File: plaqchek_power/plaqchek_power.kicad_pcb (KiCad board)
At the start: 4 copper layers, 52 x 70 mm, 93 parts, among them J1 Conn_01x05, J2 Conn_01x04, J3 Barrel_Jack_Switch, J4 Conn_01x03, U1 LM5157, U2 LM43601, U8 TPS54202DDC, U9 TPS62175DQC

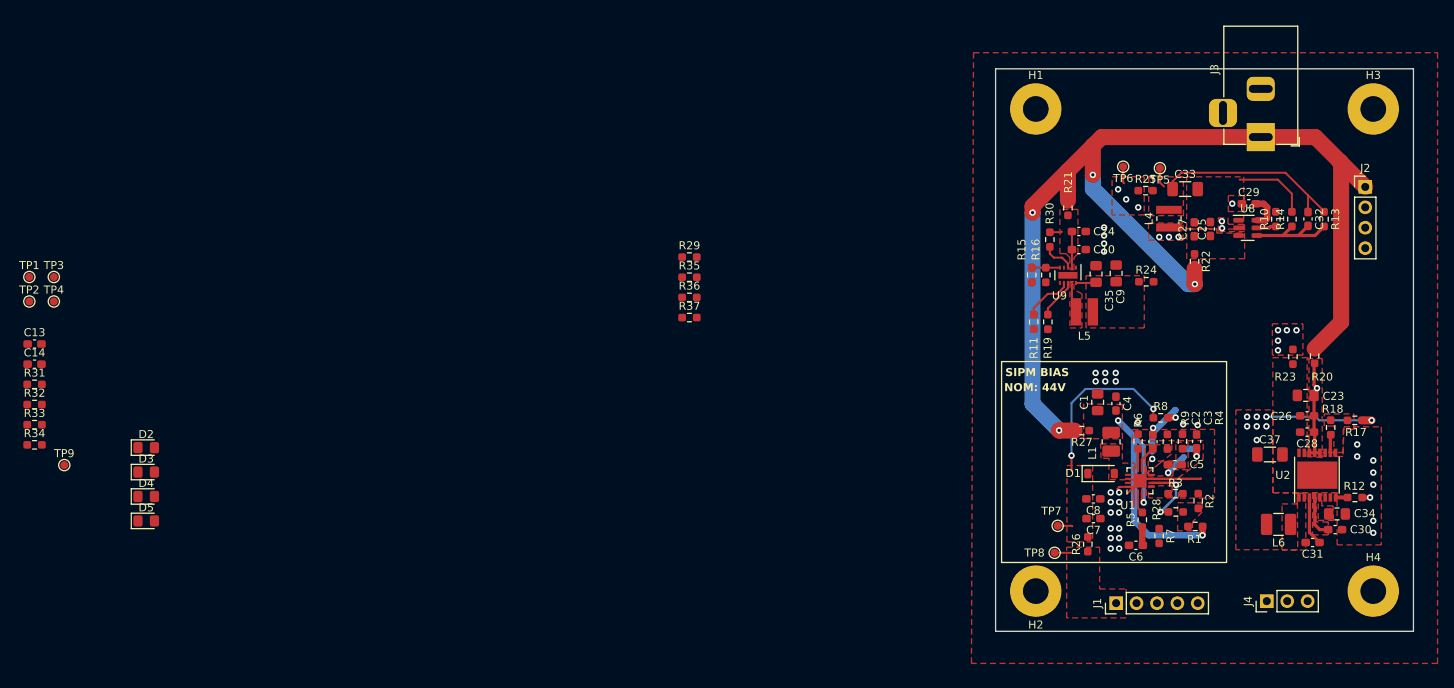
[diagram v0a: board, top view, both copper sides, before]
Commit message: minor silkscreen additions
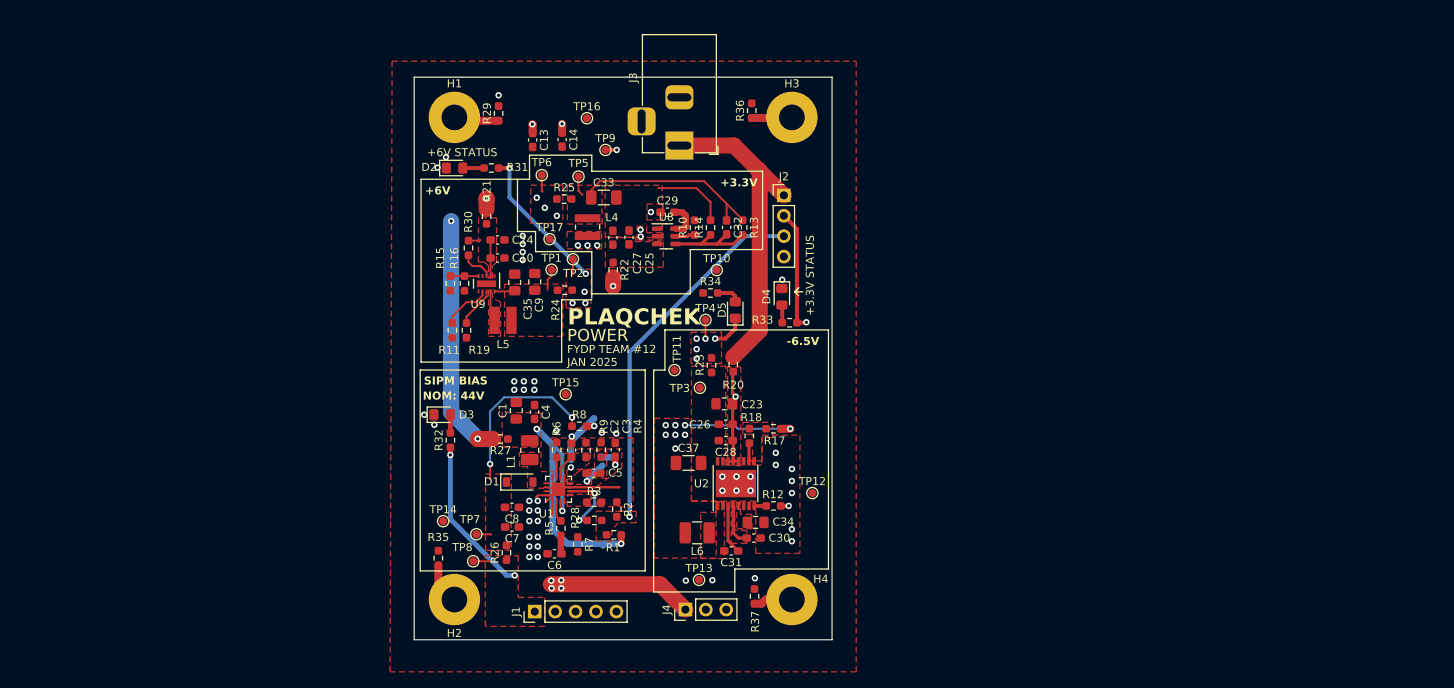
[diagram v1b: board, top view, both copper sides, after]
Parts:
- added TP10: TestPoint, TestPoint:TestPoint_Pad_D1.0mm, F.Cu at (160.3, 82.0)
- added TP11: TestPoint, TestPoint:TestPoint_Pad_D1.0mm, F.Cu at (155.1, 94.5)
- added TP12: TestPoint, TestPoint:TestPoint_Pad_D1.0mm, F.Cu at (172.2, 109.8)
- added TP13: TestPoint, TestPoint:TestPoint_Pad_D1.0mm, F.Cu at (158.1, 120.6)
- added TP14: TestPoint, TestPoint:TestPoint_Pad_D1.0mm, F.Cu at (126.2, 113.3)
- added TP15: TestPoint, TestPoint:TestPoint_Pad_D1.0mm, F.Cu at (141.5, 97.5)
- added TP16: TestPoint, TestPoint:TestPoint_Pad_D1.0mm, F.Cu at (144.2, 63.1)
- added TP17: TestPoint, TestPoint:TestPoint_Pad_D1.0mm, F.Cu at (139.5, 78.2)
- moved R33 94.8 mm to (169.4, 88.6), turned to 180 degrees
- moved R34 86.2 mm to (159.5, 84.9)
- moved D4 82.9 mm to (168.4, 85.4), turned to -90 degrees
- moved TP3 81.6 mm to (158.2, 96.7)
- moved TP4 81.1 mm to (158.9, 88.2)
- moved TP9 77.9 mm to (146.4, 67.1)
- moved D5 77.9 mm to (162.6, 87.0), turned to 90 degrees
- moved C10 72.4 mm to (133.0, 80.5)
- moved C24 72.4 mm to (133.0, 78.3)
- moved C33 72.4 mm to (146.2, 73.0)
- moved C34 72.4 mm to (165.1, 113.5)
- moved C5 72.4 mm to (144.9, 107.3)
- moved C7 72.4 mm to (134.8, 114.0)
- moved L5 72.4 mm to (133.7, 88.3)
- moved R27 72.4 mm to (133.4, 103.1)
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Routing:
- net +12V: track 132.2 -> 77.0 mm, vias 4 -> 7
- net PD_EN: track 0.00 -> 45.7 mm, vias 0 -> 1
- net +6V: track 0.00 -> 38.4 mm, vias 0 -> 9
- net SIPM_BIAS_OUT: track 2.10 -> 21.9 mm, vias 0 -> 2
- net +3V3: track 2.12 -> 17.3 mm, vias 3 -> 4
- net -6V5: track 0.00 -> 6.65 mm
- net Net-(H1-Pad1): track 0.00 -> 5.67 mm
- net Net-(H2-Pad1): track 0.00 -> 5.08 mm
- net Net-(H3-Pad1): track 0.00 -> 5.03 mm
- net Net-(H4-Pad1): track 0.00 -> 4.86 mm
- net Net-(D5-A): track 0.00 -> 3.04 mm
- net /main_pwr/VOUT_6V: track 2.53 -> 5.24 mm
- net Net-(D2-A): track 0.00 -> 2.64 mm
- net Net-(D4-A): track 0.00 -> 2.29 mm
- net Net-(D3-A): track 0.00 -> 2.25 mm
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- added copper zone on In2.Cu, net +12V
- added copper zone on F.Cu, net +6V
- added copper zone on In2.Cu, net +6V
- added copper zone on In2.Cu, net -6V5
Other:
- board text added: "+3.3V"
- board text added: "+3.3V STATUS"
- board text added: "+6V"
- board text added: "+6V STATUS"
- board text added: "-6.5V"
- board text added: "FYDP TEAM #12 JAN 2025"
- board text added: "PLAQCHEK"
- board text added: "POWER"

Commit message: finish all pcbs, generate gerber files
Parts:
- moved TP12 13.8 mm to (169.7, 96.2)
- moved TP13 9.67 mm to (166.6, 115.9)
- moved C1 2.64 mm to (134.0, 97.3)
- moved C10 2.64 mm to (131.6, 78.3)
- moved C13 2.64 mm to (136.0, 63.6)
- moved C14 2.64 mm to (139.7, 63.6)
- moved C2 2.64 mm to (140.9, 102.2)
- moved C23 2.64 mm to (159.9, 96.4)
- moved C24 2.64 mm to (131.6, 76.0)
- moved C25 2.64 mm to (148.0, 75.7)
- moved C26 2.64 mm to (160.0, 99.0)
- moved C27 2.64 mm to (146.0, 75.8)
- moved C28 2.64 mm to (160.0, 101.0)
- moved C29 2.64 mm to (152.8, 72.6)
- moved C3 2.64 mm to (146.3, 102.2)
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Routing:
- net /main_pwr/VOUT_6V: track 5.24 -> 19.9 mm, vias 0 -> 2
- net /SIPM Bias/VOUT_SIPM: track 23.4 -> 36.4 mm, vias 2 -> 4
- net /SIPM Bias/PD_BOOST_PG: track 0.00 -> 5.47 mm
- net /main_pwr/VOUT_-6V5: track 2.26 -> 5.44 mm, vias 13 -> 0
- net +12V: track 77.0 -> 74.1 mm
- net +6V: track 38.4 -> 41.0 mm, vias 9 -> 11
- net /main_pwr/VIN_-6V5: track 12.8 -> 12.5 mm, vias 1 -> 0
- net GND: vias 40 -> 181
- net (no net): vias 4 -> 0
- added copper zone on B.Cu, net /main_pwr/SW_3V3
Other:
- board text added: "-6V5"
- board text added: "12V"
- board text added: "3V3"
- board text added: "44V"
- board text added: "GND"
- board text added: "PDEN"
- board text added: "TO MLB"
- board text added: "TO POTENTIOSTAT"
- board text added: "TO SIPM SENS"
- board text removed: "+3.3V STATUS"
